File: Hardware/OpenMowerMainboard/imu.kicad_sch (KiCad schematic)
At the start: 9 parts, among them J20 Conn_01x10_Female

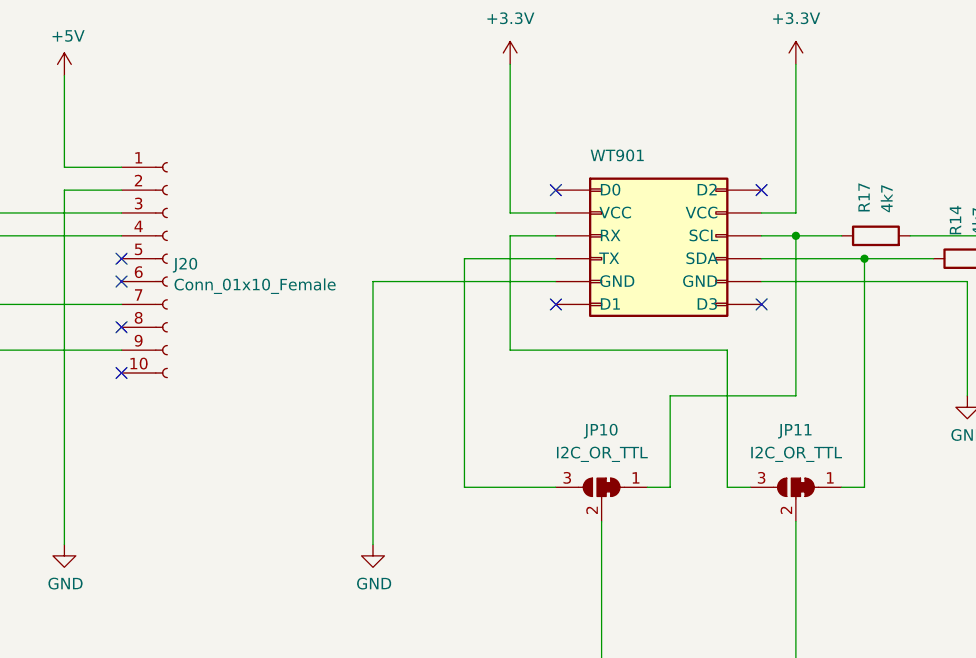
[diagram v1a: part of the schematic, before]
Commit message: feat: update to Kicad7, put back C2,C3
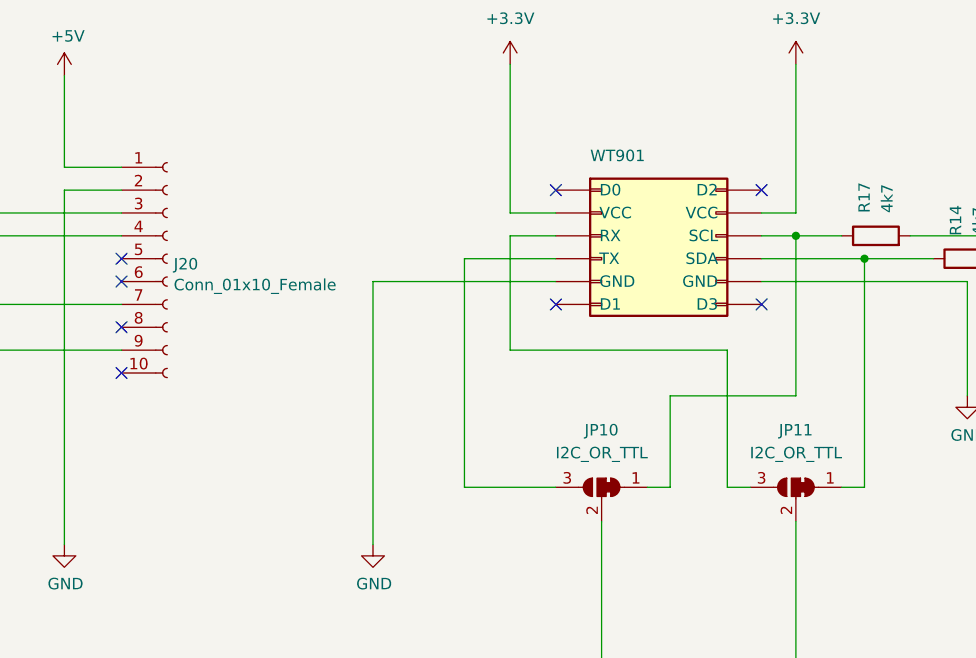
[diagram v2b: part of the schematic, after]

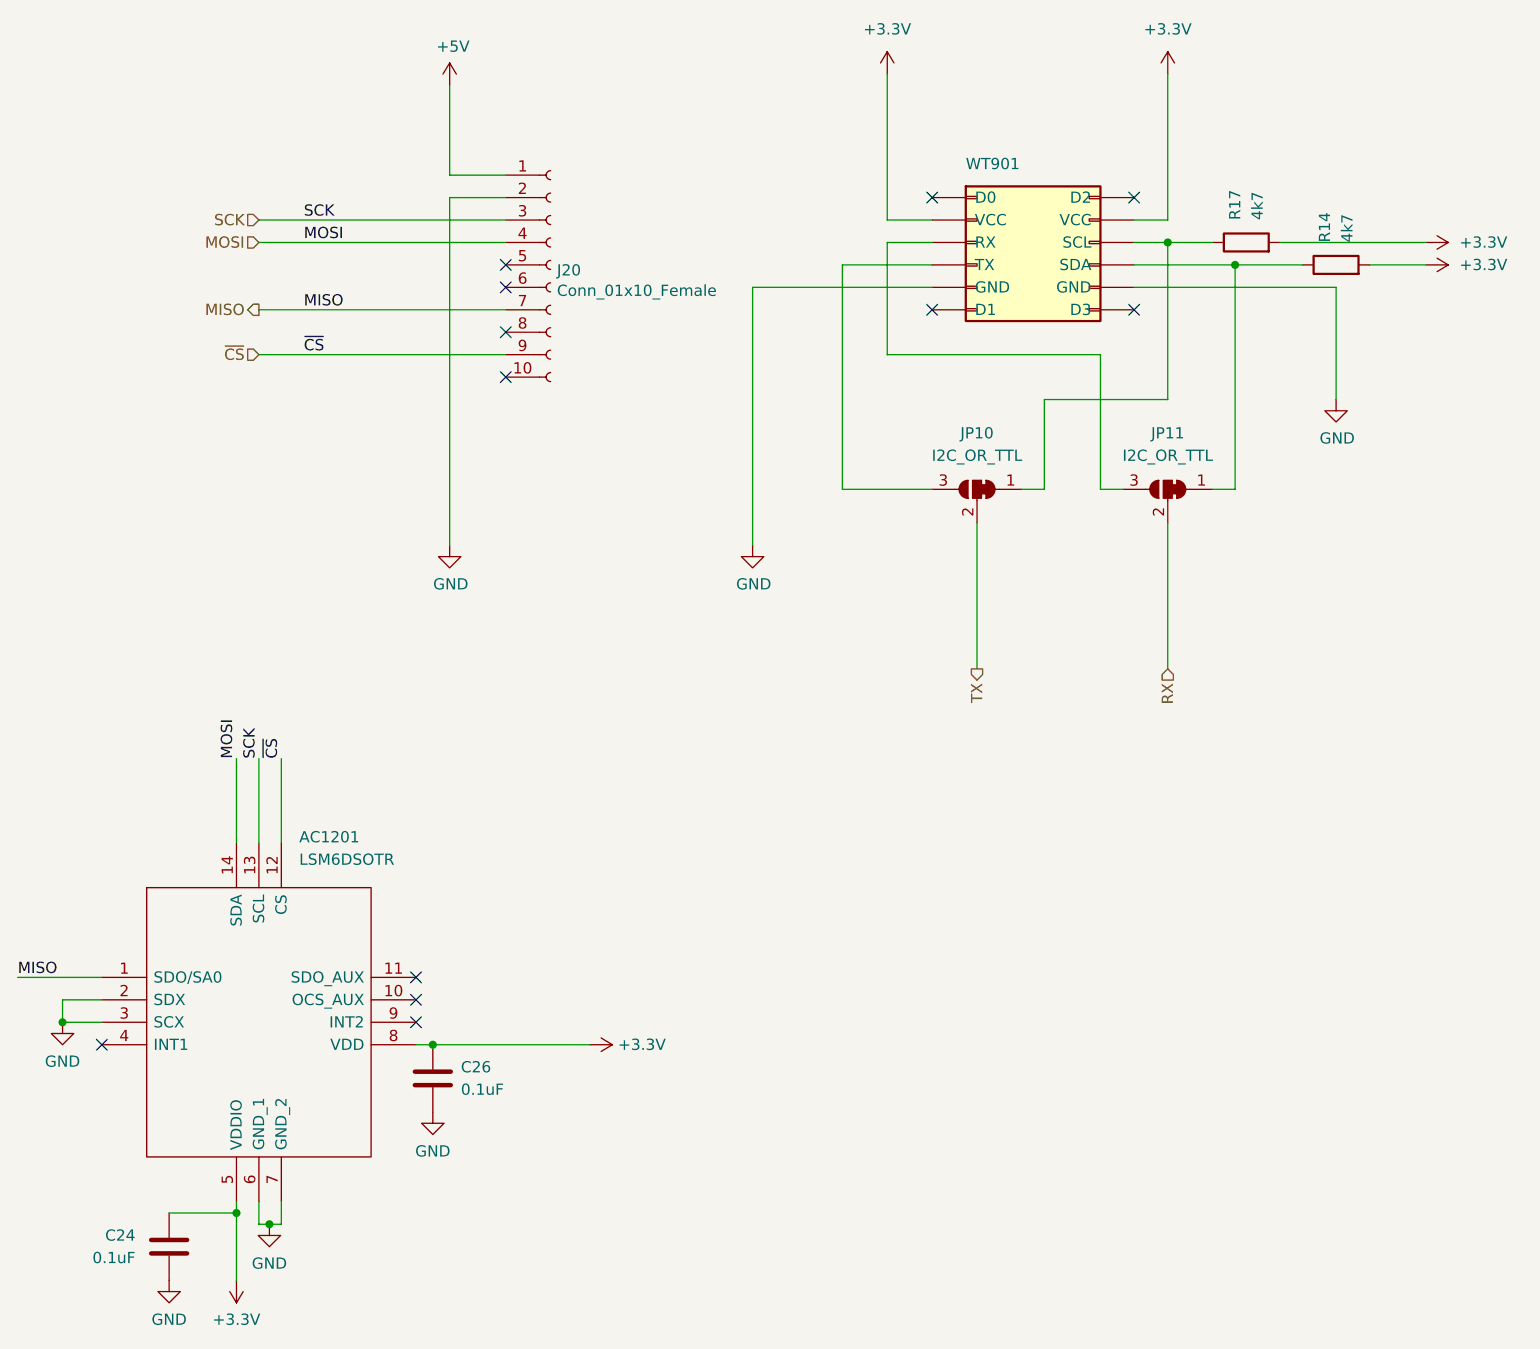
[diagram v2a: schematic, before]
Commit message: upgraded to KiCAD v8
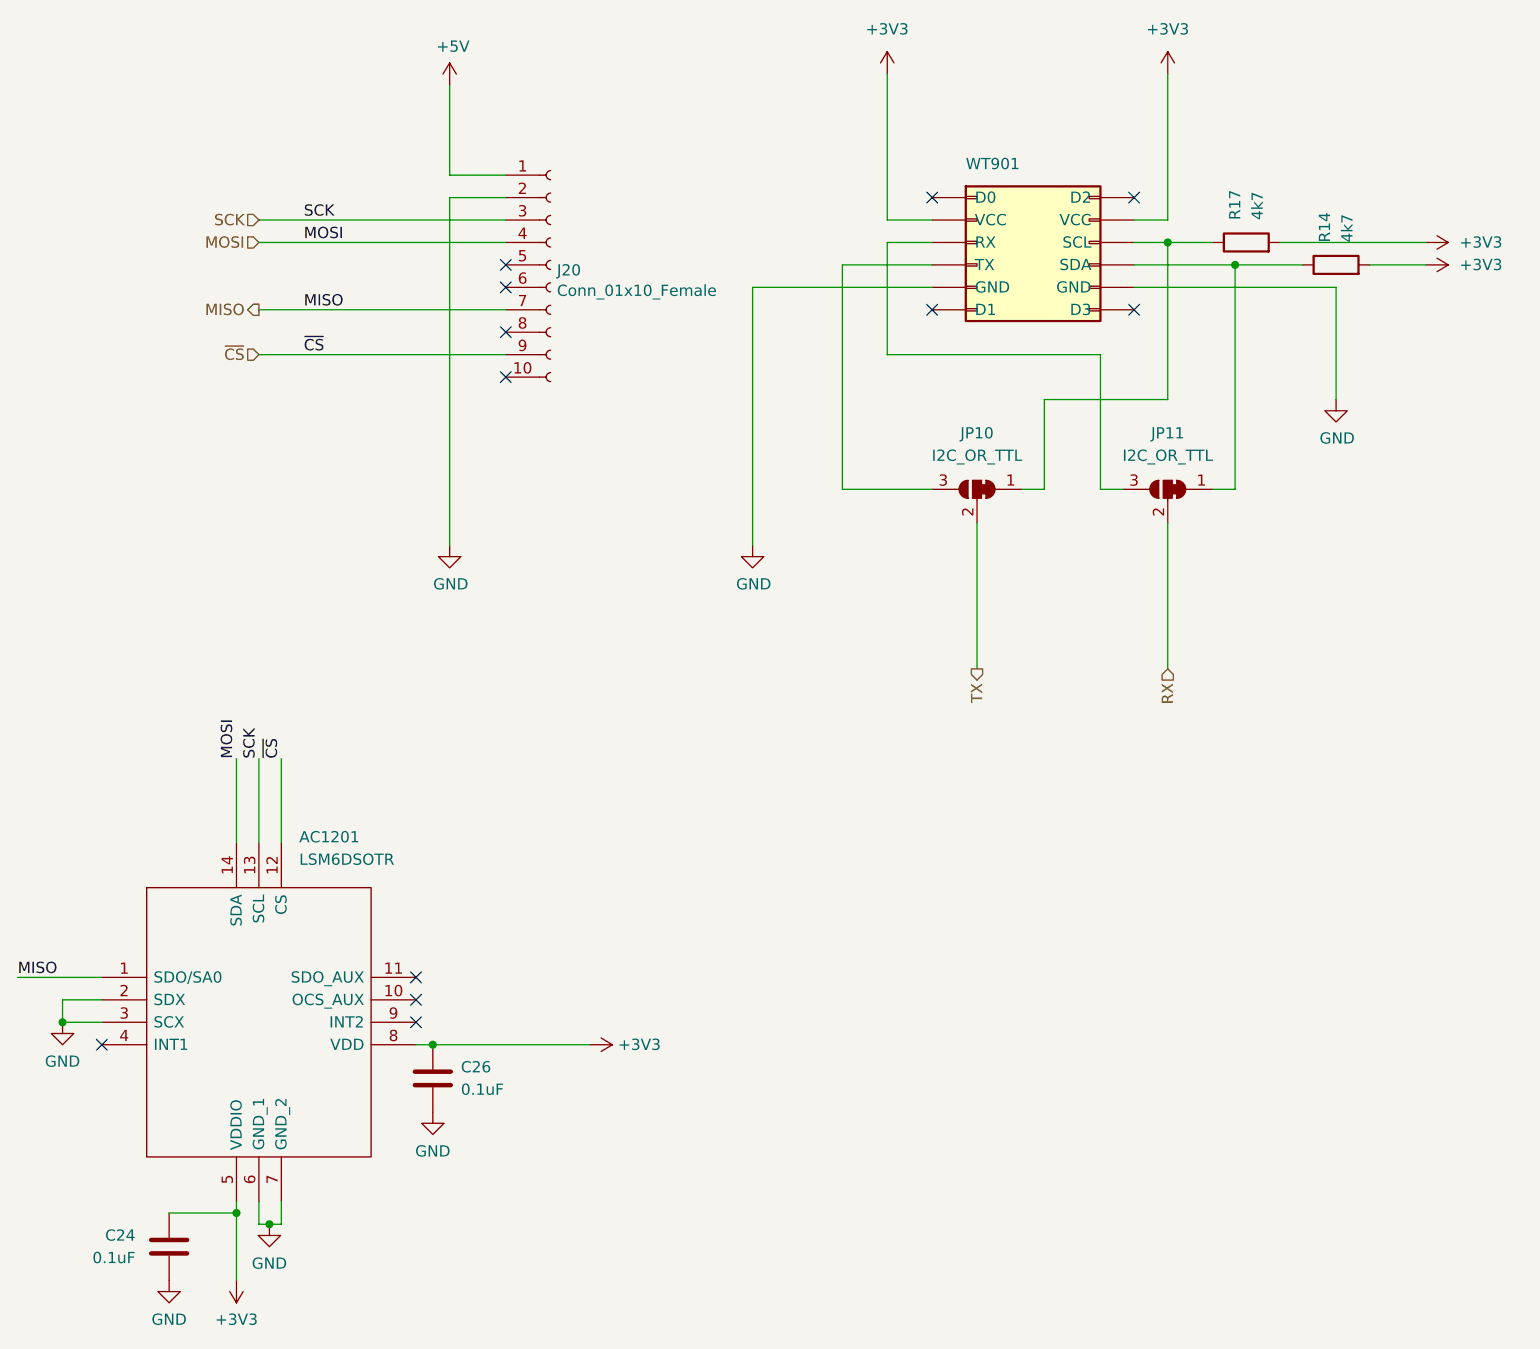
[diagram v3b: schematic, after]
